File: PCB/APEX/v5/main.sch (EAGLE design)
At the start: 4 parts

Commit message: remove double frame
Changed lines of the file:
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@@
 </classes>
 <parts>
-<part name="U$42" library="microbuilder" deviceset="FRAME_A4_ADAFRUIT" device=""/>
 <part name="JP2" library="microbuilder" deviceset="HEADER-1X5" device="70MIL"/>
 <part name="P+1" library="microbuilder" deviceset="VCC" device=""/>
@@
 <sheet>
 <plain>
-<wire x1="50.8" y1="99.06" x2="50.8" y2="101.6" width="0.1524" layer="94" style="shortdash"/>
 </plain>
 <instances>
-<instance part="U$42" gate="G$1" x="-48.26" y="48.26" smashed="yes"/>
 <instance part="JP2" gate="A" x="-5.031390625" y="611.38649375" smashed="yes" rot="R180">
 <attribute name="NAME" x="1.318609375" y="603.13149375" size="1.778" layer="95" rot="R180"/>
@@
 <pinref part="JP6" gate="A" pin="7"/>
 <pinref part="SUPPLY1" gate="+5V" pin="+5V"/>
-<label x="-63.5" y="627.38" size="1.27" layer="95" xref="yes"/>
+<label x="-66.04" y="624.84" size="1.27" layer="95" xref="yes"/>
 </segment>
 <segment>
 <pinref part="CN1" gate="G$1" pin="2"/>
 <wire x1="-81.28" y1="629.92" x2="-88.9" y2="629.92" width="0.1524" layer="91"/>
-<label x="-81.28" y="624.84" size="1.27" layer="95" xref="yes"/>
+<label x="-86.36" y="627.38" size="1.27" layer="95" rot="R270" xref="yes"/>
 </segment>
 </net>

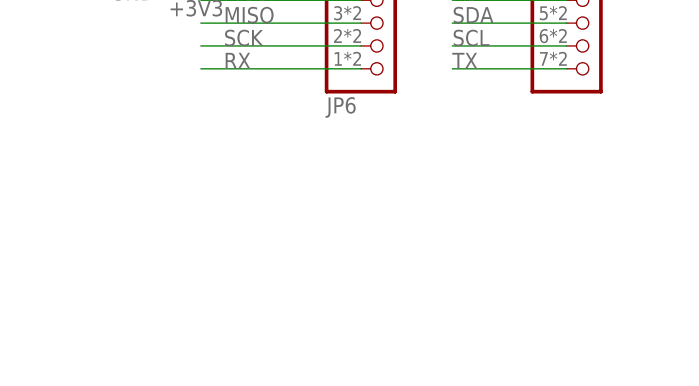
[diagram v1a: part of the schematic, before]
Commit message: introduce test points, rotate mcu for better usb pos
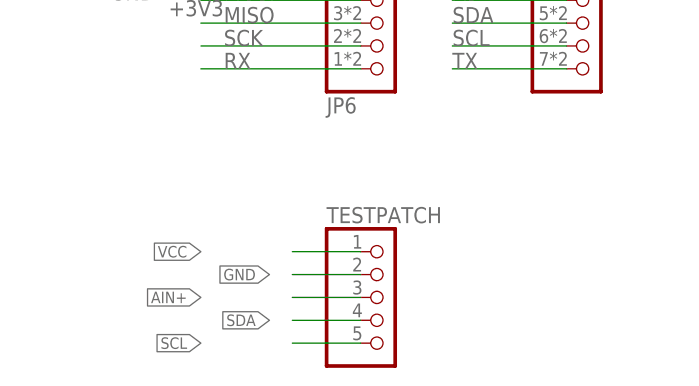
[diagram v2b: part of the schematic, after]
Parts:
- added TESTPATCH: (no value), pinhead:PINHD-1X5
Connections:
- net AIN+: now also TESTPATCH.3
- net GND: now also TESTPATCH.2
- net SCL: now also TESTPATCH.5
- net SDA: now also TESTPATCH.4
- net VCC: now also TESTPATCH.1
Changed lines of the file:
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@@
 <setting verticaltext="up"/>
 </settings>
-<grid distance="0.1" unitdist="inch" unit="inch" style="lines" multiple="1" display="no" altdistance="0.01" altunitdist="inch" altunit="inch"/>
+<grid distance="0.1" unitdist="inch" unit="inch" style="lines" multiple="1" display="yes" altdistance="0.01" altunitdist="inch" altunit="inch"/>
 <layers>
 <layer number="1" name="Top" color="4" fill="1" visible="no" active="no"/>
@@
 <part name="+3V1" library="supply1" library_urn="urn:adsk.eagle:library:371" deviceset="+3V3" device=""/>
 <part name="CN1" library="adafruit" deviceset="JST_2PIN" device="-THM"/>
+<part name="TESTPATCH" library="pinhead" library_urn="urn:adsk.eagle:library:325" deviceset="PINHD-1X5" device="" package3d_urn="urn:adsk.eagle:package:22469/2"/>
 </parts>
 <sheets>
@@
 <attribute name="VALUE" x="-85.09" y="624.84" size="1.778" layer="96"/>
 </instance>
+<instance part="TESTPATCH" gate="A" x="-48.26" y="579.12" smashed="yes">
+<attribute name="NAME" x="-54.61" y="587.375" size="1.778" layer="95"/>
+<attribute name="VALUE" x="-54.61" y="568.96" size="1.778" layer="96"/>
+</instance>
 </instances>
 <busses>
@@
 <label x="-86.36" y="627.38" size="1.27" layer="95" rot="R270" xref="yes"/>
 </segment>
+<segment>
+<pinref part="TESTPATCH" gate="A" pin="1"/>
+<wire x1="-50.8" y1="584.2" x2="-58.42" y2="584.2" width="0.1524" layer="91"/>
+<label x="-68.58" y="584.2" size="1.27" layer="95" rot="R180" xref="yes"/>
+</segment>
 </net>
 <net name="GND" class="0">
@@
 <label x="2.588609375" y="613.92649375" size="1.778" layer="95"/>
 </segment>
+<segment>
+<pinref part="TESTPATCH" gate="A" pin="2"/>
+<wire x1="-50.8" y1="581.66" x2="-58.42" y2="581.66" width="0.1524" layer="91"/>
+<label x="-60.96" y="581.66" size="1.27" layer="95" rot="R180" xref="yes"/>
+</segment>
 </net>
 <net name="SD" class="0">
@@
 <wire x1="-40.64" y1="619.76" x2="-27.94" y2="619.76" width="0.1524" layer="91"/>
 </segment>
+<segment>
+<pinref part="TESTPATCH" gate="A" pin="3"/>
+<wire x1="-50.8" y1="579.12" x2="-58.42" y2="579.12" width="0.1524" layer="91"/>
+<label x="-68.58" y="579.12" size="1.27" layer="95" rot="R180" xref="yes"/>
+</segment>
 </net>
 <net name="MOSI" class="0">
@@
 <label x="-40.64" y="607.06" size="1.778" layer="95"/>
 </segment>
+<segment>
+<pinref part="TESTPATCH" gate="A" pin="5"/>
+<wire x1="-50.8" y1="574.04" x2="-58.42" y2="574.04" width="0.1524" layer="91"/>
+<label x="-68.58" y="574.04" size="1.27" layer="95" rot="R180" xref="yes"/>
+</segment>
 </net>
 <net name="SDA" class="0">
@@
 <wire x1="-40.64" y1="609.6" x2="-27.94" y2="609.6" width="0.1524" layer="91"/>
 <label x="-40.64" y="609.6" size="1.778" layer="95"/>
+</segment>
+<segment>
+<pinref part="TESTPATCH" gate="A" pin="4"/>
+<wire x1="-50.8" y1="576.58" x2="-58.42" y2="576.58" width="0.1524" layer="91"/>
+<label x="-60.96" y="576.58" size="1.27" layer="95" rot="R180" xref="yes"/>
 </segment>
 </net>
@@
 will not be understood (or retained) with this version.
 </note>
+<note version="8.3" severity="warning">
+Since Version 8.3, EAGLE supports the association of 3D packages
+with devices in libraries, schematics, and board files. Those 3D
+packages will not be understood (or retained) with this version.
+</note>
 </compatibility>

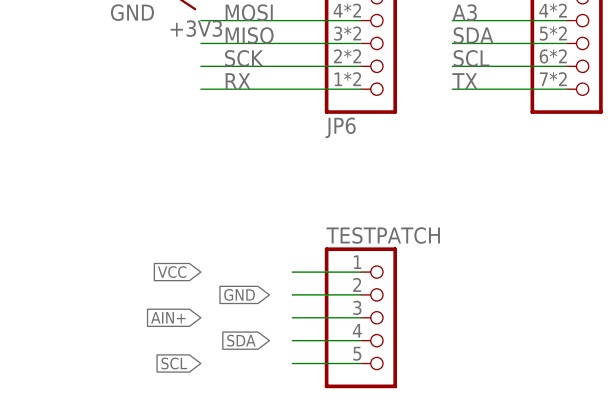
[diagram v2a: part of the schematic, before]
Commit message: swap testpoints for easier routing
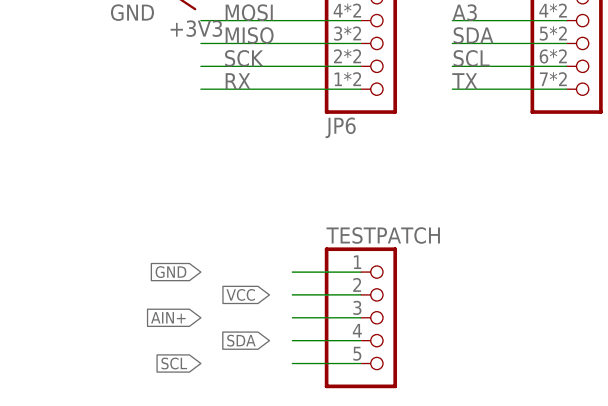
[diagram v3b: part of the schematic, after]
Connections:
- net GND: now also TESTPATCH.1; no longer TESTPATCH.2
- net VCC: now also TESTPATCH.2; no longer TESTPATCH.1
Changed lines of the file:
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@@
 </segment>
 <segment>
-<pinref part="TESTPATCH" gate="A" pin="1"/>
-<wire x1="-50.8" y1="584.2" x2="-58.42" y2="584.2" width="0.1524" layer="91"/>
-<label x="-68.58" y="584.2" size="1.27" layer="95" rot="R180" xref="yes"/>
+<pinref part="TESTPATCH" gate="A" pin="2"/>
+<wire x1="-50.8" y1="581.66" x2="-58.42" y2="581.66" width="0.1524" layer="91"/>
+<label x="-60.96" y="581.66" size="1.27" layer="95" rot="R180" xref="yes"/>
 </segment>
 </net>
@@
 </segment>
 <segment>
-<pinref part="TESTPATCH" gate="A" pin="2"/>
-<wire x1="-50.8" y1="581.66" x2="-58.42" y2="581.66" width="0.1524" layer="91"/>
-<label x="-60.96" y="581.66" size="1.27" layer="95" rot="R180" xref="yes"/>
+<pinref part="TESTPATCH" gate="A" pin="1"/>
+<wire x1="-50.8" y1="584.2" x2="-58.42" y2="584.2" width="0.1524" layer="91"/>
+<label x="-68.58" y="584.2" size="1.27" layer="95" rot="R180" xref="yes"/>
 </segment>
 </net>

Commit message: update rp2040 from new design block
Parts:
- removed JP6: (no value), microbuilder:HEADER-1X7_CASTEL
- added JP4: (no value), microbuilder:HEADER-1X7
- JP5: device microbuilder:HEADER-1X7_CASTEL -> microbuilder:HEADER-1X7
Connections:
- net +3V3: now also JP5.5; no longer JP6.5
- net A1: now also JP4.2; no longer JP5.2
- net A2: now also JP4.3; no longer JP5.3
- net A3: now also JP4.4; no longer JP5.4
- net AIN+: now also JP4.1; no longer JP5.1
- net GND: now also JP5.6; no longer JP6.6
- net MISO: now also JP5.3; no longer JP6.3
- net MOSI: now also JP5.4; no longer JP6.4
- net RX: now also JP5.1; no longer JP6.1
- net SCK: now also JP5.2; no longer JP6.2
- net SCL: now also JP4.6; no longer JP5.6
- net SDA: now also JP4.5; no longer JP5.5
- net TX: now also JP4.7; no longer JP5.7
- net VCC: now also JP5.7; no longer JP6.7
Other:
- note added: "amp"
- note added: "bat"
- note added: "rp2040"
- moved on the sheet: JP5

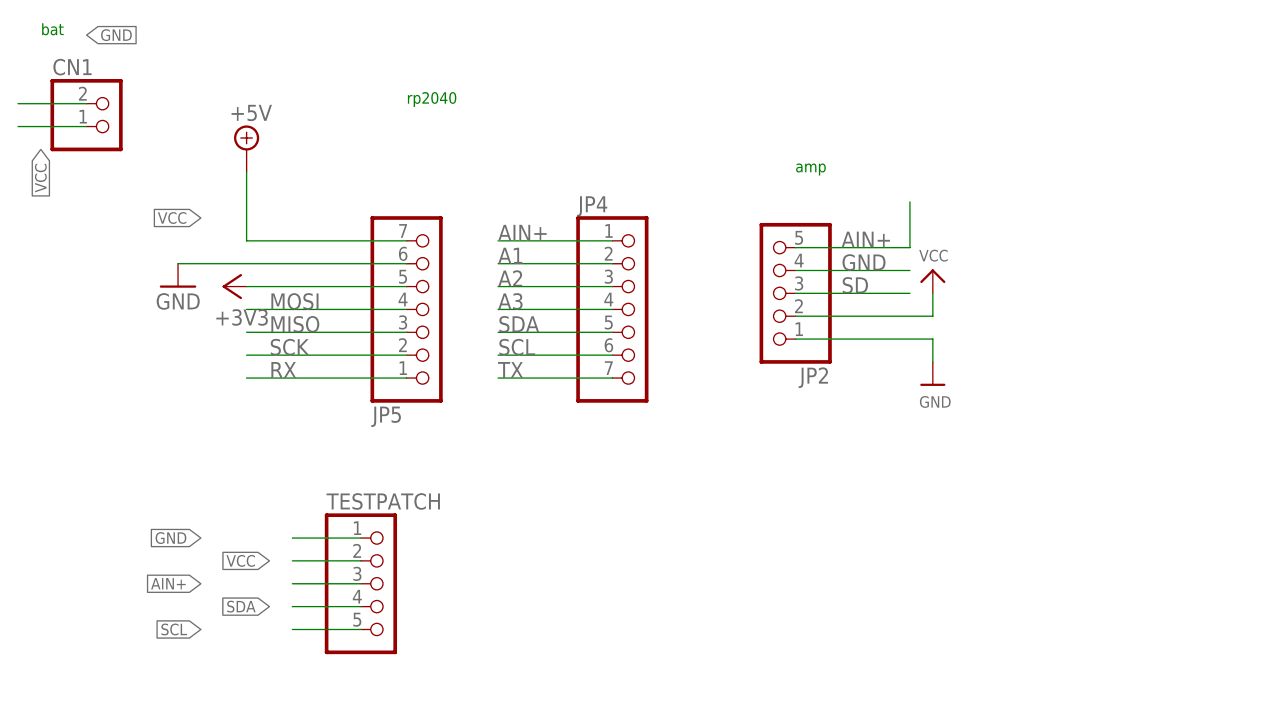
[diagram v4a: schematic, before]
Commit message: add STM 1n5819 to schematic
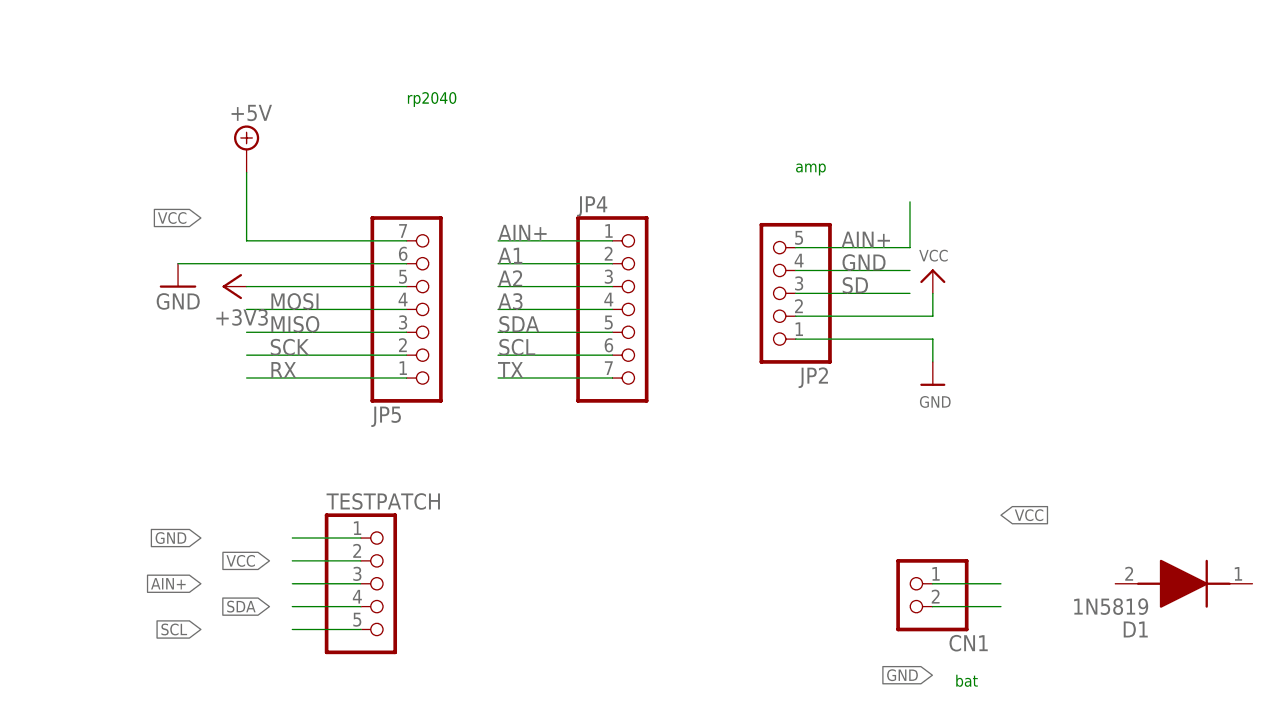
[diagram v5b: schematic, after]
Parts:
- added D1: 1N5819, SamacSys_Parts:1N5819
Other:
- moved on the sheet: CN1
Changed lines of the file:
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@@
 <part name="SUPPLY1" library="supply2" library_urn="urn:adsk.eagle:library:372" deviceset="+5V" device=""/>
 <part name="+3V1" library="supply1" library_urn="urn:adsk.eagle:library:371" deviceset="+3V3" device=""/>
+<part name="D1" library="SamacSys_Parts" deviceset="1N5819" device=""/>
 </parts>
 <sheets>
@@
 <plain>
 <text x="-2.54" y="624.84" size="1.27" layer="91">amp</text>
-<text x="-86.36" y="640.08" size="1.27" layer="91">bat</text>
+<text x="17.78" y="568.96" size="1.27" layer="91" rot="R180">bat</text>
 <text x="-45.72" y="632.46" size="1.27" layer="91">rp2040</text>
 </plain>
@@
 </instance>
 <instance part="U$3" gate="G$1" x="-93.98" y="469.9" smashed="yes"/>
-<instance part="CN1" gate="G$1" x="-78.74" y="629.92" smashed="yes">
-<attribute name="NAME" x="-85.09" y="635.635" size="1.778" layer="95"/>
-<attribute name="VALUE" x="-85.09" y="624.84" size="1.778" layer="96"/>
+<instance part="CN1" gate="G$1" x="10.16" y="579.12" smashed="yes" rot="R180">
+<attribute name="NAME" x="19.05" y="573.405" size="1.778" layer="95" rot="R180"/>
+<attribute name="VALUE" x="16.51" y="584.2" size="1.778" layer="96" rot="R180"/>
 </instance>
 <instance part="TESTPATCH" gate="A" x="-48.26" y="579.12" smashed="yes">
@@
 <attribute name="VALUE" x="-60.96" y="609.6" size="1.778" layer="96" rot="R180"/>
 </instance>
+<instance part="D1" gate="G$1" x="48.26" y="579.12" smashed="yes" rot="R180">
+<attribute name="NAME" x="36.83" y="574.04" size="1.778" layer="95" rot="R180" align="center-left"/>
+<attribute name="VALUE" x="36.83" y="576.58" size="1.778" layer="96" rot="R180" align="center-left"/>
+</instance>
 </instances>
 <busses>
@@
 <segment>
 <pinref part="CN1" gate="G$1" pin="2"/>
-<wire x1="-81.28" y1="629.92" x2="-88.9" y2="629.92" width="0.1524" layer="91"/>
-<label x="-86.36" y="627.38" size="1.27" layer="95" rot="R270" xref="yes"/>
+<wire x1="12.7" y1="579.12" x2="20.32" y2="579.12" width="0.1524" layer="91"/>
+<label x="20.32" y="586.74" size="1.27" layer="95" xref="yes"/>
 </segment>
 <segment>
@@
 <segment>
 <pinref part="CN1" gate="G$1" pin="1"/>
-<wire x1="-81.28" y1="632.46" x2="-88.9" y2="632.46" width="0.1524" layer="91"/>
-<label x="-81.28" y="640.08" size="1.27" layer="95" xref="yes"/>
+<wire x1="12.7" y1="576.58" x2="20.32" y2="576.58" width="0.1524" layer="91"/>
+<label x="12.7" y="568.96" size="1.27" layer="95" rot="R180" xref="yes"/>
 </segment>
 <segment>

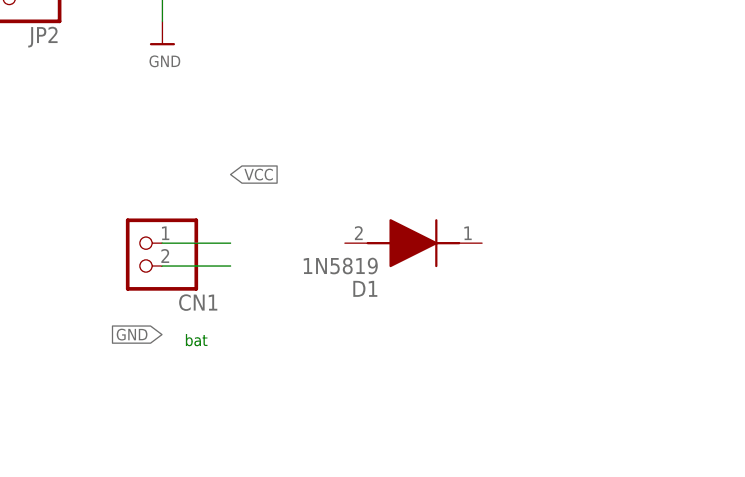
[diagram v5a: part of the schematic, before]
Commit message: connect schottky
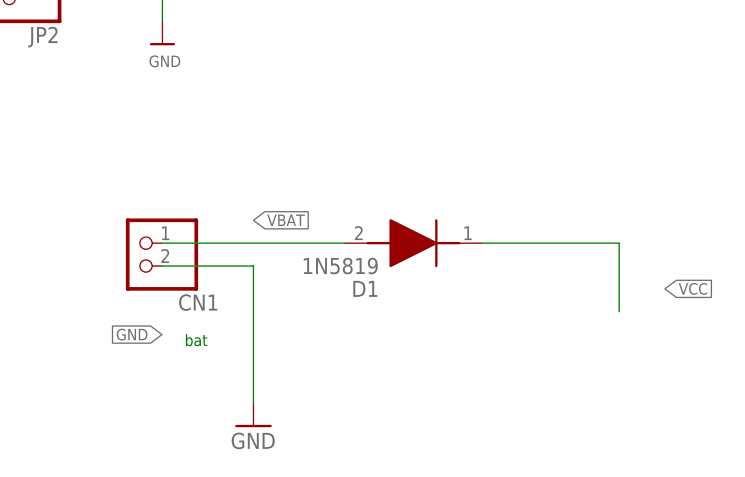
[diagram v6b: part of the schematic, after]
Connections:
- new net VBAT: CN1.2, D1.A
- net VCC: now also D1.K; no longer CN1.2
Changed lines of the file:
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@@
 <part name="+3V1" library="supply1" library_urn="urn:adsk.eagle:library:371" deviceset="+3V3" device=""/>
 <part name="D1" library="SamacSys_Parts" deviceset="1N5819" device=""/>
+<part name="GND2" library="supply1" library_urn="urn:adsk.eagle:library:371" deviceset="GND" device=""/>
 </parts>
 <sheets>
@@
 <attribute name="VALUE" x="36.83" y="576.58" size="1.778" layer="96" rot="R180" align="center-left"/>
 </instance>
+<instance part="GND2" gate="1" x="22.86" y="558.8" smashed="yes">
+<attribute name="VALUE" x="20.32" y="556.26" size="1.778" layer="96"/>
+</instance>
 </instances>
 <busses>
@@
 </segment>
 <segment>
-<pinref part="CN1" gate="G$1" pin="2"/>
-<wire x1="12.7" y1="579.12" x2="20.32" y2="579.12" width="0.1524" layer="91"/>
-<label x="20.32" y="586.74" size="1.27" layer="95" xref="yes"/>
-</segment>
-<segment>
 <pinref part="TESTPATCH" gate="A" pin="2"/>
 <wire x1="-50.8" y1="581.66" x2="-58.42" y2="581.66" width="0.1524" layer="91"/>
@@
 <label x="-68.58" y="619.76" size="1.27" layer="95" rot="R180" xref="yes"/>
 </segment>
+<segment>
+<pinref part="D1" gate="G$1" pin="K"/>
+<wire x1="48.26" y1="579.12" x2="63.5" y2="579.12" width="0.1524" layer="91"/>
+<wire x1="63.5" y1="579.12" x2="63.5" y2="571.5" width="0.1524" layer="91"/>
+<label x="68.58" y="574.04" size="1.27" layer="95" xref="yes"/>
+</segment>
 </net>
 <net name="GND" class="0">
@@
 <segment>
 <pinref part="CN1" gate="G$1" pin="1"/>
-<wire x1="12.7" y1="576.58" x2="20.32" y2="576.58" width="0.1524" layer="91"/>
+<wire x1="12.7" y1="576.58" x2="22.86" y2="576.58" width="0.1524" layer="91"/>
 <label x="12.7" y="568.96" size="1.27" layer="95" rot="R180" xref="yes"/>
+<wire x1="22.86" y1="576.58" x2="22.86" y2="561.34" width="0.1524" layer="91"/>
+<pinref part="GND2" gate="1" pin="GND"/>
 </segment>
 <segment>
@@
 </segment>
 </net>
+<net name="VBAT" class="0">
+<segment>
+<pinref part="CN1" gate="G$1" pin="2"/>
+<label x="22.86" y="581.66" size="1.27" layer="95" xref="yes"/>
+<pinref part="D1" gate="G$1" pin="A"/>
+<wire x1="12.7" y1="579.12" x2="33.02" y2="579.12" width="0.1524" layer="91"/>
+</segment>
+</net>
